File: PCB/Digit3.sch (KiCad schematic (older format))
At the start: 1 part

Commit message: Worked on PCB.
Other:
- moved on the sheet: D3C
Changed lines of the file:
@@
 L LED_Array D3
 U 3 1 54BC7666
-P 5000 4100
-F 0 "D3" H 5000 5250 50  0000 C CNN
-F 1 "LED_Array" H 5000 5350 50  0000 C CNN
-F 2 "Custom:LED-ARRAY" H 5000 5025 50  0001 C CNN
-F 3 "" H 5000 5025 50  0000 C CNN
-	3    5000 4100
+P 3750 4150
+F 0 "D3" H 3750 5300 50  0000 C CNN
+F 1 "LED_Array" H 3750 5400 50  0000 C CNN
+F 2 "Custom:LED-ARRAY" H 3750 5075 50  0001 C CNN
+F 3 "" H 3750 5075 50  0000 C CNN
+	3    3750 4150
 	1    0    0    -1
 $EndComp

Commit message: Updated schematic.
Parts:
- added Q? (x14): FDG1024NZ, SC70-6, symbol FDG1024NZ
- added R? (x14): 10K, symbol R
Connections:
- net labels added: D2A1, D2A2, D2A3, D2A4, D2A5, D2A6, D2S1G, D2S1R, D2S2G, D2S2R, D2S3G, D2S3R, D2S4G, D2S4R, D2S5G, D2S5R, D2S6G, D2S6R, D2S7G, D2S7R, GND
- wire segments 0 -> 257
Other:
- moved on the sheet: D3C

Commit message: Updated schematic.
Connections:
- net labels added: D3A1, D3A2, D3A3, D3A4, D3A5, D3A6, D3S1G, D3S1R, D3S2G, D3S2R, D3S3G, D3S3R, D3S4G, D3S4R, D3S5G, D3S5R, D3S6G, D3S6R, D3S7G, D3S7R
- net labels removed: D2A1, D2A2, D2A3, D2A4, D2A5, D2A6, D2S1G, D2S1R, D2S2G, D2S2R, D2S3G, D2S3R, D2S4G, D2S4R, D2S5G, D2S5R, D2S6G, D2S6R, D2S7G, D2S7R

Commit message: Updated mosfets.
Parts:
- removed Q? (x14): FDG1024NZ, SC70-6, symbol FDG1024NZ
- added Q? (x14): DMN2041LSD-13, SO-8, symbol DMN2041LSD-13
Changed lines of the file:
@@
 D3A6
-$Comp
-L FDG1024NZ Q?
-U 1 1 54EB2DCB
-P 1350 2350
-F 0 "Q?" H 1350 2201 40  0000 R CNN
-F 1 "FDG1024NZ" H 1350 2500 40  0000 R CNN
-F 2 "SC70-6" H 1220 2452 29  0000 C CNN
-F 3 "" H 1350 2350 60  0000 C CNN
-	1    1350 2350
-	1    0    0    -1
-$EndComp
-$Comp
-L FDG1024NZ Q?
-U 1 1 54EB2DD2
-P 2350 2350
-F 0 "Q?" H 2350 2201 40  0000 R CNN
-F 1 "FDG1024NZ" H 2350 2500 40  0000 R CNN
-F 2 "SC70-6" H 2220 2452 29  0000 C CNN
-F 3 "" H 2350 2350 60  0000 C CNN
-	1    2350 2350
-	1    0    0    -1
-$EndComp
 $Comp
 L R R?
@@
 $EndComp
 $Comp
-L FDG1024NZ Q?
-U 1 1 54EB2DF3
-P 1350 5050
-F 0 "Q?" H 1350 4901 40  0000 R CNN
-F 1 "FDG1024NZ" H 1350 5200 40  0000 R CNN
-F 2 "SC70-6" H 1220 5152 29  0000 C CNN
-F 3 "" H 1350 5050 60  0000 C CNN
-	1    1350 5050
-	1    0    0    -1
-$EndComp
-$Comp
 L R R?
 U 1 1 54EB2DFA
@@
 D3S5G
 $Comp
-L FDG1024NZ Q?
-U 1 1 54EB2E18
-P 2350 5050
-F 0 "Q?" H 2350 4901 40  0000 R CNN
-F 1 "FDG1024NZ" H 2350 5200 40  0000 R CNN
-F 2 "SC70-6" H 2220 5152 29  0000 C CNN
-F 3 "" H 2350 5050 60  0000 C CNN
-	1    2350 5050
-	1    0    0    -1
-$EndComp
-$Comp
-L FDG1024NZ Q?
-U 1 1 54EB2E1F
-P 1350 6825
-F 0 "Q?" H 1350 6676 40  0000 R CNN
-F 1 "FDG1024NZ" H 1350 6975 40  0000 R CNN
-F 2 "SC70-6" H 1220 6927 29  0000 C CNN
-F 3 "" H 1350 6825 60  0000 C CNN
-	1    1350 6825
-	1    0    0    -1
-$EndComp
-$Comp
 L R R?
 U 1 1 54EB2E26
@@
 Text HLabel 1900 6875 0    50   Input ~ 0
 D3S4G
-$Comp
-L FDG1024NZ Q?
-U 1 1 54EB2E42
-P 2350 6825
-F 0 "Q?" H 2350 6676 40  0000 R CNN
-F 1 "FDG1024NZ" H 2350 6975 40  0000 R CNN
-F 2 "SC70-6" H 2220 6927 29  0000 C CNN
-F 3 "" H 2350 6825 60  0000 C CNN
-	1    2350 6825
-	1    0    0    -1
-$EndComp
 Wire Wire Line
 	3705 1150 3705 950
@@
 Wire Wire Line
 	2450 6625 2450 6500
-$Comp
-L FDG1024NZ Q?
-U 1 1 54EB2F5D
-P 7700 1125
-F 0 "Q?" H 7700 976 40  0000 R CNN
-F 1 "FDG1024NZ" H 7700 1275 40  0000 R CNN
-F 2 "SC70-6" H 7570 1227 29  0000 C CNN
-F 3 "" H 7700 1125 60  0000 C CNN
-	1    7700 1125
-	1    0    0    -1
-$EndComp
 $Comp
 L R R?
@@
 Text HLabel 8250 1175 0    50   Input ~ 0
 D3S1G
-$Comp
-L FDG1024NZ Q?
-U 1 1 54EB2F80
-P 8700 1125
-F 0 "Q?" H 8700 976 40  0000 R CNN
-F 1 "FDG1024NZ" H 8700 1275 40  0000 R CNN
-F 2 "SC70-6" H 8570 1227 29  0000 C CNN
-F 3 "" H 8700 1125 60  0000 C CNN
-	1    8700 1125
-	1    0    0    -1
-$EndComp
 Wire Wire Line
 	8250 1175 8500 1175
@@
 Wire Wire Line
 	8800 675  8800 925
-$Comp
-L FDG1024NZ Q?
-U 1 1 54EB2F96
-P 7700 2625
-F 0 "Q?" H 7700 2476 40  0000 R CNN
-F 1 "FDG1024NZ" H 7700 2775 40  0000 R CNN
-F 2 "SC70-6" H 7570 2727 29  0000 C CNN
-F 3 "" H 7700 2625 60  0000 C CNN
-	1    7700 2625
-	1    0    0    -1
-$EndComp
 $Comp
 L R R?
@@
 Text HLabel 8250 2675 0    50   Input ~ 0
 D3S2G
-$Comp
-L FDG1024NZ Q?
-U 1 1 54EB2FB9
-P 8700 2625
-F 0 "Q?" H 8700 2476 40  0000 R CNN
-F 1 "FDG1024NZ" H 8700 2775 40  0000 R CNN
-F 2 "SC70-6" H 8570 2727 29  0000 C CNN
-F 3 "" H 8700 2625 60  0000 C CNN
-	1    8700 2625
-	1    0    0    -1
-$EndComp
 Wire Wire Line
 	8250 2675 8500 2675
@@
 Wire Wire Line
 	8800 2125 8800 2425
-$Comp
-L FDG1024NZ Q?
-U 1 1 54EB2FD0
-P 7700 5485
-F 0 "Q?" H 7700 5336 40  0000 R CNN
-F 1 "FDG1024NZ" H 7700 5635 40  0000 R CNN
-F 2 "SC70-6" H 7570 5587 29  0000 C CNN
-F 3 "" H 7700 5485 60  0000 C CNN
-	1    7700 5485
-	1    0    0    -1
-$EndComp
 $Comp
 L R R?
@@
 Text HLabel 8250 5535 0    50   Input ~ 0
 D3S3G
-$Comp
-L FDG1024NZ Q?
-U 1 1 54EB2FF3
-P 8700 5485
-F 0 "Q?" H 8700 5336 40  0000 R CNN
-F 1 "FDG1024NZ" H 8700 5635 40  0000 R CNN
-F 2 "SC70-6" H 8570 5587 29  0000 C CNN
-F 3 "" H 8700 5485 60  0000 C CNN
-	1    8700 5485
-	1    0    0    -1
-$EndComp
 Wire Wire Line
 	8250 5535 8500 5535
@@
 Wire Wire Line
 	7800 750  7800 925
-$Comp
-L FDG1024NZ Q?
-U 1 1 54EB300B
-P 7700 4010
-F 0 "Q?" H 7700 3861 40  0000 R CNN
-F 1 "FDG1024NZ" H 7700 4160 40  0000 R CNN
-F 2 "SC70-6" H 7570 4112 29  0000 C CNN
-F 3 "" H 7700 4010 60  0000 C CNN
-	1    7700 4010
-	1    0    0    -1
-$EndComp
 $Comp
 L R R?
@@
 Text HLabel 8250 4060 0    50   Input ~ 0
 D3S7G
-$Comp
-L FDG1024NZ Q?
-U 1 1 54EB302E
-P 8700 4010
-F 0 "Q?" H 8700 3861 40  0000 R CNN
-F 1 "FDG1024NZ" H 8700 4160 40  0000 R CNN
-F 2 "SC70-6" H 8570 4112 29  0000 C CNN
-F 3 "" H 8700 4010 60  0000 C CNN
-	1    8700 4010
-	1    0    0    -1
-$EndComp
 Wire Wire Line
 	8250 4060 8500 4060
@@
 EndData
 $EndBitmap
+$Comp
+L DMN2041LSD-13 Q?
+U 1 1 54EDBF06
+P 1350 2350
+F 0 "Q?" H 1350 2201 40  0000 R CNN
+F 1 "DMN2041LSD-13" H 1350 2500 40  0000 R CNN
+F 2 "SO-8" H 1220 2452 29  0001 C CNN
+F 3 "" H 1350 2350 60  0000 C CNN
+	1    1350 2350
+	1    0    0    -1
+$EndComp
+$Comp
+L DMN2041LSD-13 Q?
+U 2 1 54EDBF6F
+P 2350 2350
+F 0 "Q?" H 2350 2201 40  0000 R CNN
+F 1 "DMN2041LSD-13" H 2350 2500 40  0000 R CNN
+F 2 "SO-8" H 2220 2452 29  0001 C CNN
+F 3 "" H 2350 2350 60  0000 C CNN
+	2    2350 2350
+	1    0    0    -1
+$EndComp
+$Comp
+L DMN2041LSD-13 Q?
+U 1 1 54EDC37A
+P 1350 5050
+F 0 "Q?" H 1350 4901 40  0000 R CNN
+F 1 "DMN2041LSD-13" H 1350 5200 40  0000 R CNN
+F 2 "SO-8" H 1220 5152 29  0001 C CNN
+F 3 "" H 1350 5050 60  0000 C CNN
+	1    1350 5050
+	1    0    0    -1
+$EndComp
+$Comp
+L DMN2041LSD-13 Q?
+U 2 1 54EDC3E5
+P 2350 5050
+F 0 "Q?" H 2350 4901 40  0000 R CNN
+F 1 "DMN2041LSD-13" H 2350 5200 40  0000 R CNN
+F 2 "SO-8" H 2220 5152 29  0001 C CNN
+F 3 "" H 2350 5050 60  0000 C CNN
+	2    2350 5050
+	1    0    0    -1
+$EndComp
+$Comp
+L DMN2041LSD-13 Q?
+U 1 1 54EDC6C3
+P 1350 6825
+F 0 "Q?" H 1350 6676 40  0000 R CNN
+F 1 "DMN2041LSD-13" H 1350 6975 40  0000 R CNN
+F 2 "SO-8" H 1220 6927 29  0001 C CNN
+F 3 "" H 1350 6825 60  0000 C CNN
+	1    1350 6825
+	1    0    0    -1
+$EndComp
+$Comp
+L DMN2041LSD-13 Q?
+U 2 1 54EDC724
+P 2350 6825
+F 0 "Q?" H 2350 6676 40  0000 R CNN
+F 1 "DMN2041LSD-13" H 2350 6975 40  0000 R CNN
+F 2 "SO-8" H 2220 6927 29  0001 C CNN
+F 3 "" H 2350 6825 60  0000 C CNN
+	2    2350 6825
+	1    0    0    -1
+$EndComp
+$Comp
+L DMN2041LSD-13 Q?
+U 1 1 54EDCABE
+P 7700 5485
+F 0 "Q?" H 7700 5336 40  0000 R CNN
+F 1 "DMN2041LSD-13" H 7700 5635 40  0000 R CNN
+F 2 "SO-8" H 7570 5587 29  0001 C CNN
+F 3 "" H 7700 5485 60  0000 C CNN
+	1    7700 5485
+	1    0    0    -1
+$EndComp
+$Comp
+L DMN2041LSD-13 Q?
+U 2 1 54EDCB1D
+P 8700 5485
+F 0 "Q?" H 8700 5336 40  0000 R CNN
+F 1 "DMN2041LSD-13" H 8700 5635 40  0000 R CNN
+F 2 "SO-8" H 8570 5587 29  0001 C CNN
+F 3 "" H 8700 5485 60  0000 C CNN
+	2    8700 5485
+	1    0    0    -1
+$EndComp
+$Comp
+L DMN2041LSD-13 Q?
+U 1 1 54EDCFD5
+P 7700 4010
+F 0 "Q?" H 7700 3861 40  0000 R CNN
+F 1 "DMN2041LSD-13" H 7700 4160 40  0000 R CNN
+F 2 "SO-8" H 7570 4112 29  0001 C CNN
+F 3 "" H 7700 4010 60  0000 C CNN
+	1    7700 4010
+	1    0    0    -1
+$EndComp
+$Comp
+L DMN2041LSD-13 Q?
+U 2 1 54EDD024
+P 8700 4010
+F 0 "Q?" H 8700 3861 40  0000 R CNN
+F 1 "DMN2041LSD-13" H 8700 4160 40  0000 R CNN
+F 2 "SO-8" H 8570 4112 29  0001 C CNN
+F 3 "" H 8700 4010 60  0000 C CNN
+	2    8700 4010
+	1    0    0    -1
+$EndComp
+$Comp
+L DMN2041LSD-13 Q?
+U 1 1 54EDD4CE
+P 7700 2625
+F 0 "Q?" H 7700 2476 40  0000 R CNN
+F 1 "DMN2041LSD-13" H 7700 2775 40  0000 R CNN
+F 2 "SO-8" H 7570 2727 29  0001 C CNN
+F 3 "" H 7700 2625 60  0000 C CNN
+	1    7700 2625
+	1    0    0    -1
+$EndComp
+$Comp
+L DMN2041LSD-13 Q?
+U 2 1 54EDD52B
+P 8700 2625
+F 0 "Q?" H 8700 2476 40  0000 R CNN
+F 1 "DMN2041LSD-13" H 8700 2775 40  0000 R CNN
+F 2 "SO-8" H 8570 2727 29  0001 C CNN
+F 3 "" H 8700 2625 60  0000 C CNN
+	2    8700 2625
+	1    0    0    -1
+$EndComp
+$Comp
+L DMN2041LSD-13 Q?
+U 1 1 54EDDB35
+P 7700 1125
+F 0 "Q?" H 7700 976 40  0000 R CNN
+F 1 "DMN2041LSD-13" H 7700 1275 40  0000 R CNN
+F 2 "SO-8" H 7570 1227 29  0001 C CNN
+F 3 "" H 7700 1125 60  0000 C CNN
+	1    7700 1125
+	1    0    0    -1
+$EndComp
+$Comp
+L DMN2041LSD-13 Q?
+U 2 1 54EDDB98
+P 8700 1125
+F 0 "Q?" H 8700 976 40  0000 R CNN
+F 1 "DMN2041LSD-13" H 8700 1275 40  0000 R CNN
+F 2 "SO-8" H 8570 1227 29  0001 C CNN
+F 3 "" H 8700 1125 60  0000 C CNN
+	2    8700 1125
+	1    0    0    -1
+$EndComp
 $EndSCHEMATC

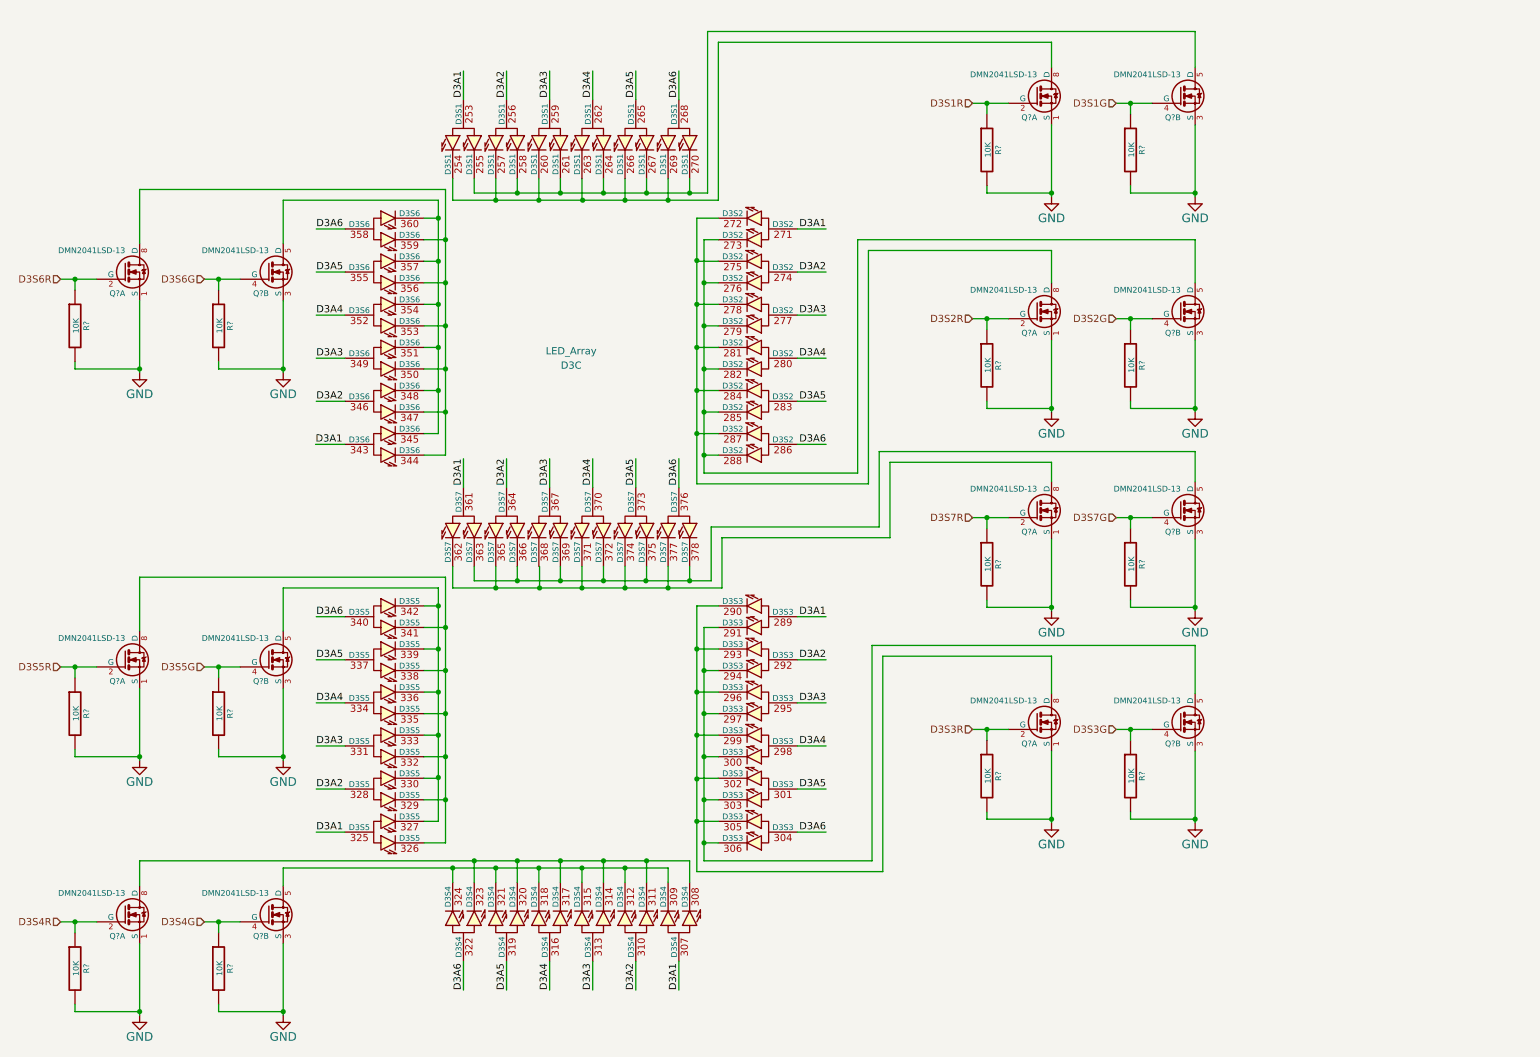
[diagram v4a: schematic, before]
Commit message: Added additional mosfets.
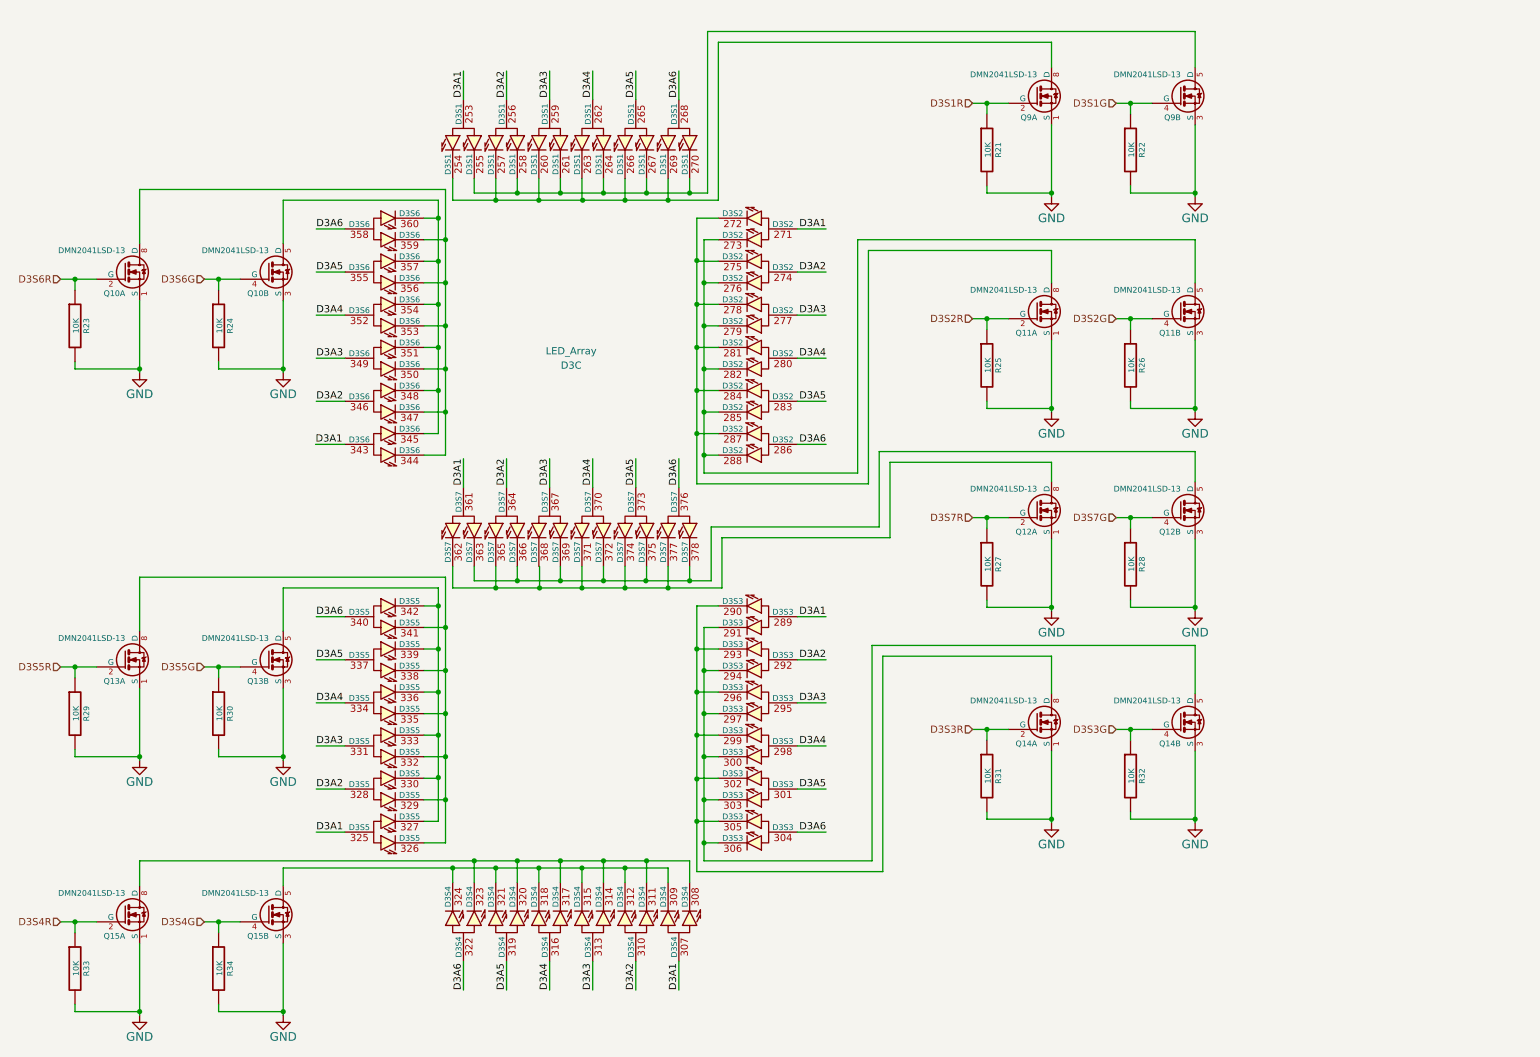
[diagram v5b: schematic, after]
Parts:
- Q10, Q11, Q12, Q13, Q14, Q15, Q9: renamed from Q?; footprint SO-8 -> Power_Integrations:SO-8
- R21, R22, R23, R24, R25, R26, R27, R28, R29, R30, R31, R32, R33, R34: renamed from R?; footprint (none) -> Resistors_SMD:R_0603_HandSoldering

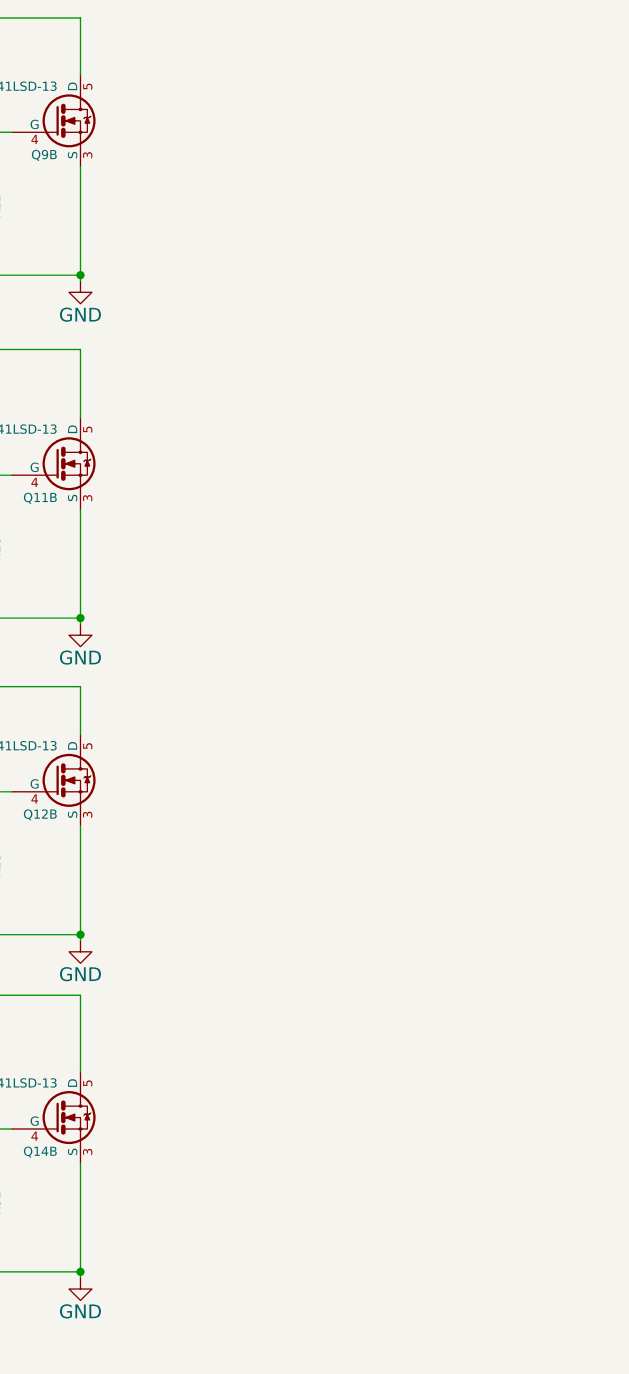
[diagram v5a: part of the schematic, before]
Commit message: Added additional mosfets.
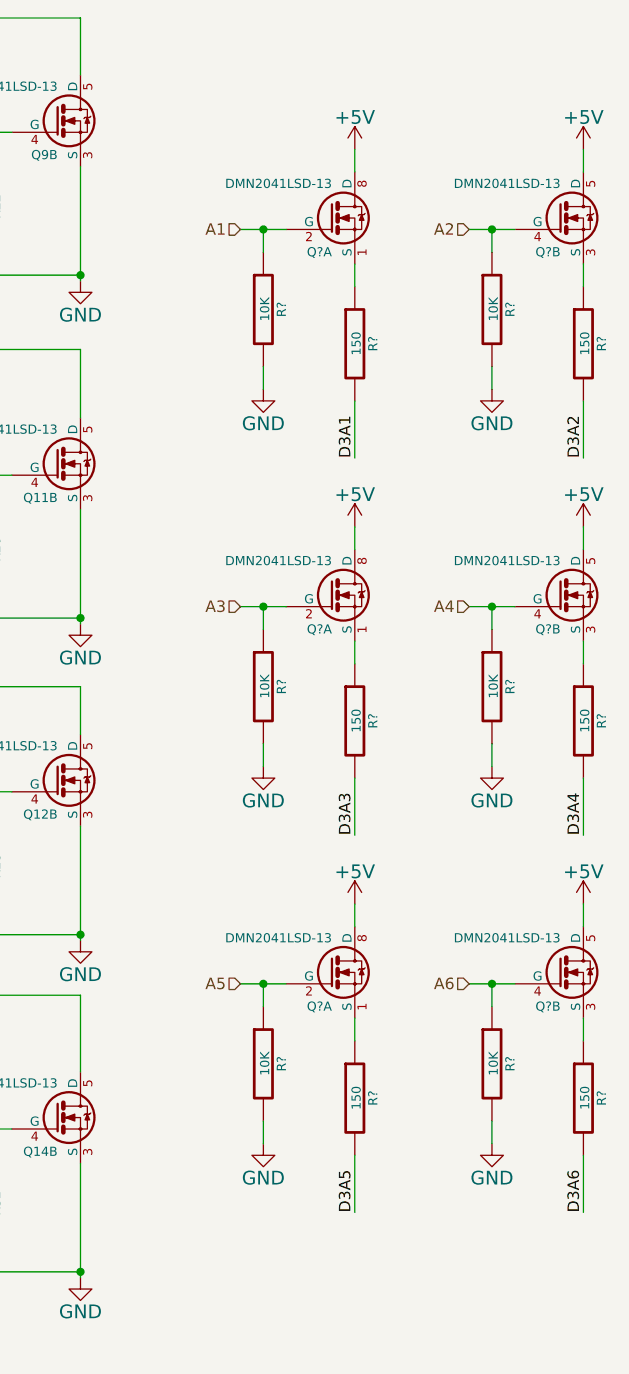
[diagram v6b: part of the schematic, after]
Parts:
- added Q? (x6): DMN2041LSD-13, SO-8, symbol DMN2041LSD-13
- added R? (x6): 10K, Resistors_SMD:R_0603_HandSoldering, symbol R
- added R? (x6): 150, Resistors_SMD:R_0603_HandSoldering, symbol R
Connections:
- net D3A1: now also R?.2
- net D3A2: now also R?.2
- net D3A3: now also R?.2
- net D3A4: now also R?.2
- net D3A5: now also R?.2
- net D3A6: now also R?.2
- net GND: now also R?.2, R?.2, R?.2, R?.2, R?.2, R?.2
- new net: Q?.1 (S), R?.1 (x3)
- new net: Q?.3 (S), R?.1 (x3)
- new net +5V: Q?.5 (D), Q?.5 (D), Q?.5 (D), Q?.8 (D), Q?.8 (D), Q?.8 (D)
- new net A1: Q?.2 (G), R?.1
- new net A2: Q?.4 (G), R?.1
- new net A3: Q?.2 (G), R?.1
- new net A4: Q?.4 (G), R?.1
- new net A5: Q?.2 (G), R?.1
- new net A6: Q?.4 (G), R?.1

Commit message: Edit PCB.
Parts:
- gave numbers to parts that had none: 15

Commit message: PCB work.
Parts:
- removed Q36, Q37, Q38: DMN2041LSD-13, SO-8, symbol DMN2041LSD-13
- removed R87, R88, R91, R92, R95, R96: 10K, Resistors_SMD:R_0603_HandSoldering, symbol R
- removed R89, R90, R93, R94, R97, R98: 150, Resistors_SMD:R_0603_HandSoldering, symbol R
- renumbered Q9 to Q19, Q10 to Q20, Q11 to Q21, Q12 to Q22, Q13 to Q23, Q14 to Q24, Q15 to Q25, R21 to R47, R22 to R48, R23 to R49, R24 to R50, R25 to R51, R26 to R52, R27 to R53, R28 to R54, R29 to R55, R30 to R56, R31 to R57, R32 to R58, R33 to R59, R34 to R60
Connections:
- net D3A1 is gone; now on net A1: D3.253 (D3S1), D3.271 (D3S2), D3.289 (D3S3), D3.307 (D3S4), D3.325 (D3S5), D3.343 (D3S6), D3.361 (D3S7)
- net D3A2 is gone; now on net A2: D3.256 (D3S1), D3.274 (D3S2), D3.292 (D3S3), D3.310 (D3S4), D3.328 (D3S5), D3.346 (D3S6), D3.364 (D3S7)
- net D3A3 is gone; now on net A3: D3.259 (D3S1), D3.277 (D3S2), D3.295 (D3S3), D3.313 (D3S4), D3.331 (D3S5), D3.349 (D3S6), D3.367 (D3S7)
- net D3A4 is gone; now on net A4: D3.262 (D3S1), D3.280 (D3S2), D3.298 (D3S3), D3.316 (D3S4), D3.334 (D3S5), D3.352 (D3S6), D3.370 (D3S7)
- net D3A5 is gone; now on net A5: D3.265 (D3S1), D3.283 (D3S2), D3.301 (D3S3), D3.319 (D3S4), D3.337 (D3S5), D3.355 (D3S6), D3.373 (D3S7)
- net D3A6 is gone; now on net A6: D3.268 (D3S1), D3.286 (D3S2), D3.304 (D3S3), D3.322 (D3S4), D3.340 (D3S5), D3.358 (D3S6), D3.376 (D3S7)
- net at D3.362 (D3S7), D3.365 (D3S7), D3.371 (D3S7)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: now also D3.368 (D3S7)
